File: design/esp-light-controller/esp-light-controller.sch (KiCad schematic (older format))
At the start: 7 parts, among them J1 WS2812b, J2 USB, Q1 2N7000, U1 LD1117V33, U2 ESP-01v090

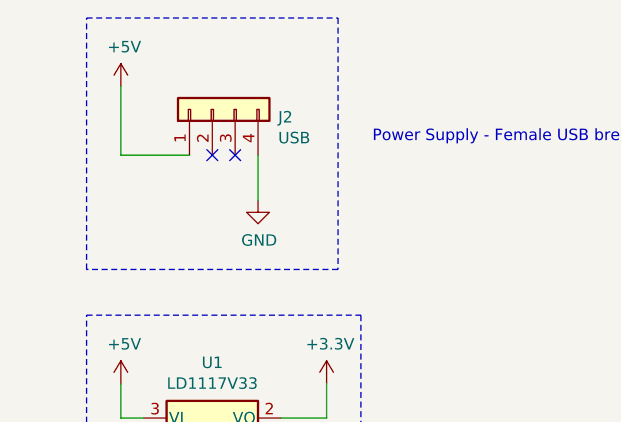
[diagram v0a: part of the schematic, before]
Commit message: Update pinout for USB connector
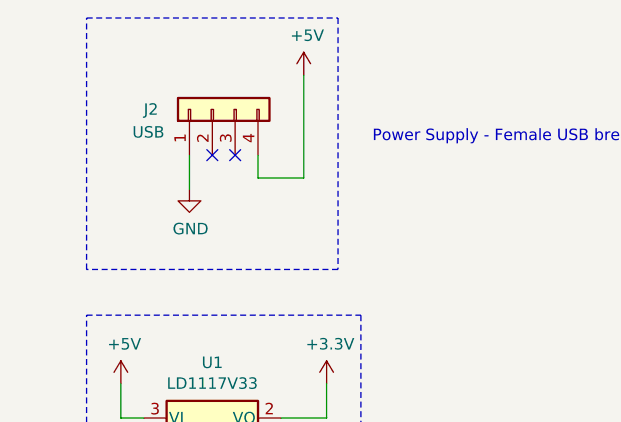
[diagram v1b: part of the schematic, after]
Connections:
- net +5V: now also J2.4 (Pin_4); no longer J2.1 (Pin_1)
- net GND: now also J2.1 (Pin_1); no longer J2.4 (Pin_4)
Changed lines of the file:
@@
 EESchema Schematic File Version 4
-LIBS:accentlights-cache
+LIBS:esp-light-controller-cache
 EELAYER 26 0
 EELAYER END
@@
 U 1 1 5C7850DB
 P 3850 1100
-F 0 "J2" V 3816 812 50  0000 R CNN
-F 1 "USB" V 3725 812 50  0000 R CNN
+F 0 "J2" V 3850 1400 50  0000 R CNN
+F 1 "USB" V 3750 1450 50  0000 R CNN
 F 2 "" H 3850 1100 50  0001 C CNN
 F 3 "~" H 3850 1100 50  0001 C CNN
@@
 L power:+5V #PWR?
 U 1 1 5C78538F
-P 3450 1000
-F 0 "#PWR?" H 3450 850 50  0001 C CNN
-F 1 "+5V" H 3465 1173 50  0000 C CNN
-F 2 "" H 3450 1000 50  0001 C CNN
-F 3 "" H 3450 1000 50  0001 C CNN
-	1    3450 1000
+P 4250 950
+F 0 "#PWR?" H 4250 800 50  0001 C CNN
+F 1 "+5V" H 4265 1123 50  0000 C CNN
+F 2 "" H 4250 950 50  0001 C CNN
+F 3 "" H 4250 950 50  0001 C CNN
+	1    4250 950
 	1    0    0    -1
 $EndComp
@@
 L power:GND #PWR?
 U 1 1 5C7853C0
-P 4050 1500
-F 0 "#PWR?" H 4050 1250 50  0001 C CNN
-F 1 "GND" H 4055 1327 50  0000 C CNN
-F 2 "" H 4050 1500 50  0001 C CNN
-F 3 "" H 4050 1500 50  0001 C CNN
-	1    4050 1500
-	1    0    0    -1
-$EndComp
-Wire Wire Line
-	3750 1300 3450 1300
-Wire Wire Line
-	3450 1300 3450 1000
-Wire Wire Line
-	4050 1300 4050 1500
+P 3750 1450
+F 0 "#PWR?" H 3750 1200 50  0001 C CNN
+F 1 "GND" H 3755 1277 50  0000 C CNN
+F 2 "" H 3750 1450 50  0001 C CNN
+F 3 "" H 3750 1450 50  0001 C CNN
+	1    3750 1450
+	1    0    0    -1
+$EndComp
 Wire Wire Line
 	3550 2450 3450 2450
@@
 Text Notes 7450 2250 0    50   ~ 0
 WS2812b JST Connector
+Wire Wire Line
+	4250 950  4250 1400
+Wire Wire Line
+	4250 1400 4050 1400
+Wire Wire Line
+	4050 1400 4050 1300
+Wire Wire Line
+	3750 1450 3750 1300
 $EndSCHEMATC
